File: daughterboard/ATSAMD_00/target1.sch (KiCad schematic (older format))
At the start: 0 parts

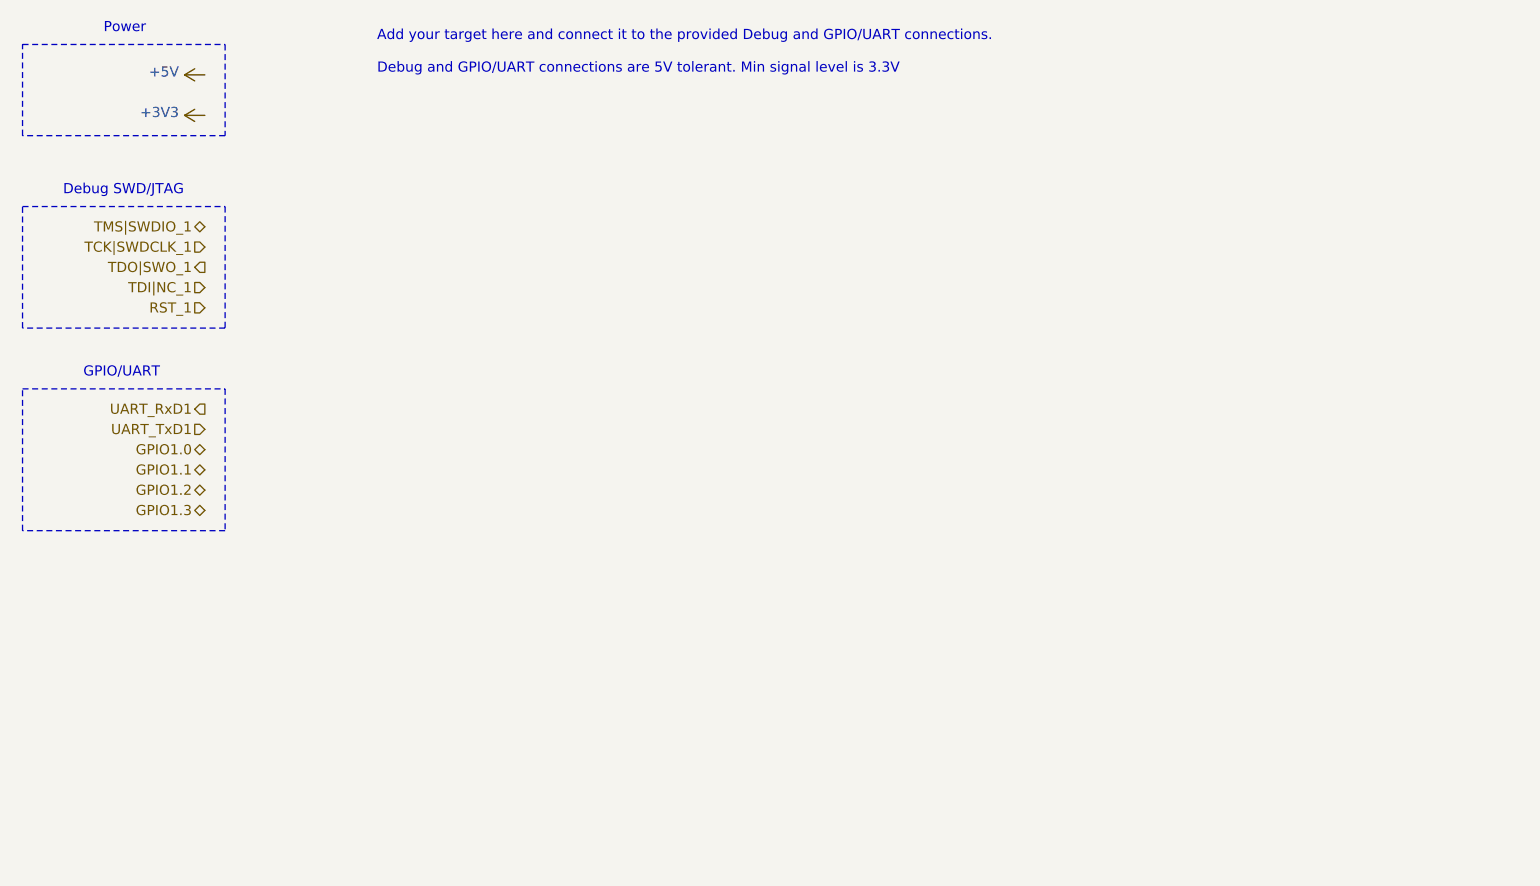
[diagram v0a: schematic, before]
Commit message: finished ATSAMD daughterboard schematics
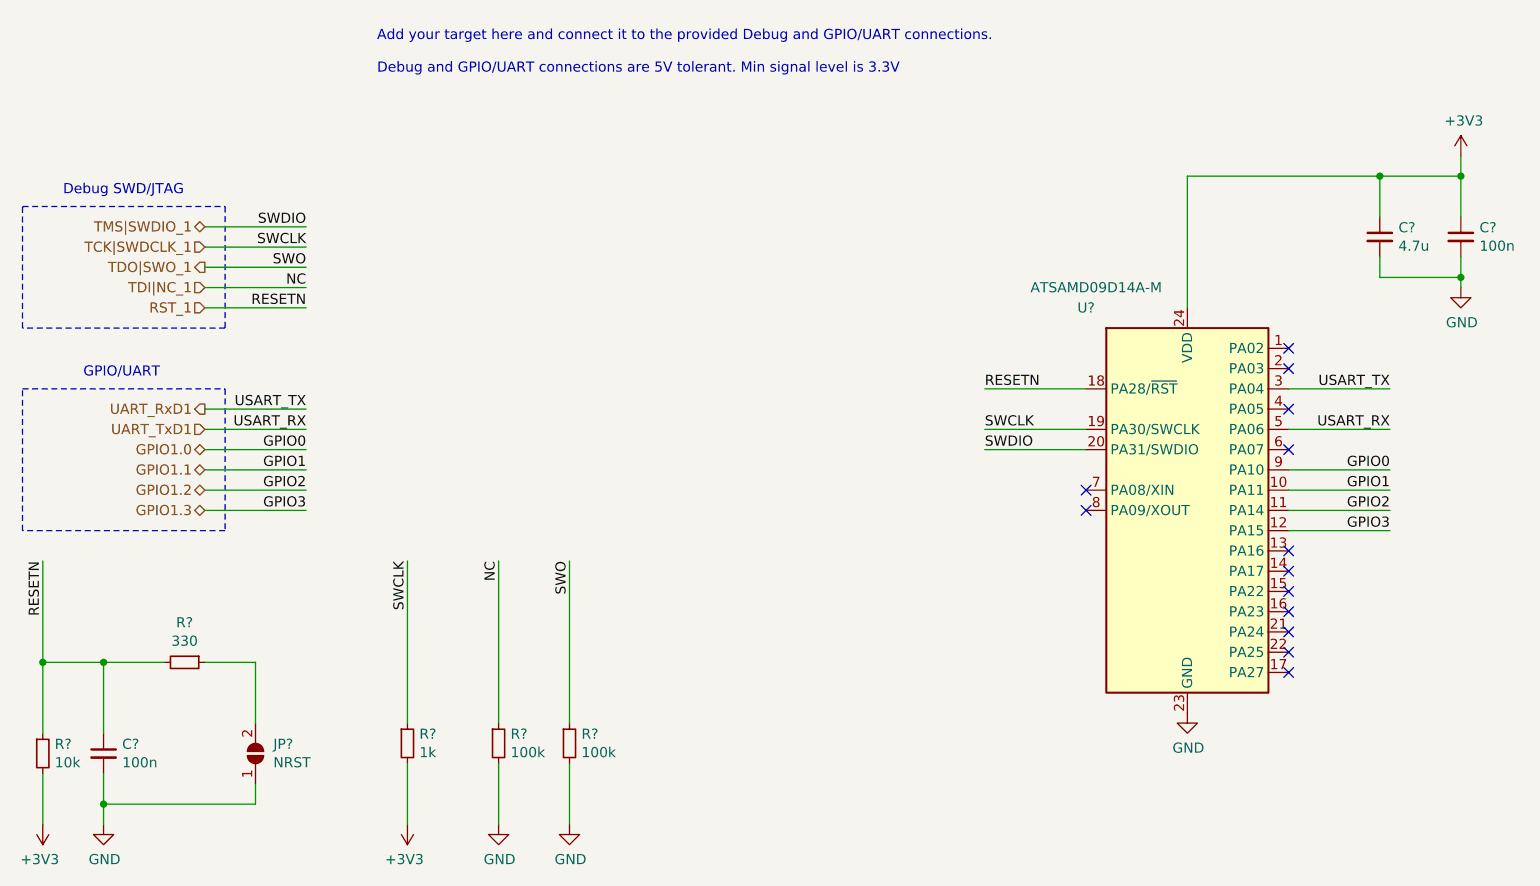
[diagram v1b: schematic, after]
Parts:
- added C?: 4.7u, symbol Device:C_Small
- added C? (x2): 100n, symbol Device:C_Small
- added JP?: NRST, symbol Jumper:SolderJumper_2_Open
- added R?: 10k, symbol Device:R_Small
- added R?: 330, symbol Device:R_Small
- added R?: 1k, symbol Device:R_Small
- added R? (x2): 100k, symbol Device:R_Small
- added U?: ATSAMD09D14A-M, Package_DFN_QFN:QFN-24-1EP_4x4mm_P0.5mm_EP2.6x2.6mm, symbol MCU_Microchip_SAMD:ATSAMD09D14A-M
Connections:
- net +3V3: now also C?.1, C?.1, R?.2, R?.2, U?.24 (VDD)
- net GPIO1.0: now also U?.9 (PA10)
- net GPIO1.1: now also U?.10 (PA11)
- net GPIO1.2: now also U?.11 (PA14)
- net GPIO1.3: now also U?.12 (PA15)
- net RST_1: now also C?.1, R?.1, R?.2, U?.18 (PA28/~RST)
- net TCK|SWDCLK_1: now also R?.1, U?.19 (PA30/SWCLK)
- net TDI|NC_1: now also R?.1
- net TDO|SWO_1: now also R?.1
- net TMS|SWDIO_1: now also U?.20 (PA31/SWDIO)
- net UART_RxD1: now also U?.3 (PA04)
- net UART_TxD1: now also U?.5 (PA06)
- new net: JP?.2 (B), R?.1
- new net GND: C?.2, C?.2, C?.2, JP?.1 (A), R?.2, R?.2, U?.23 (GND)
- no-connect marks 0 -> 13
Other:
- note removed: "Power"

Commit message: ERC on daughterboards
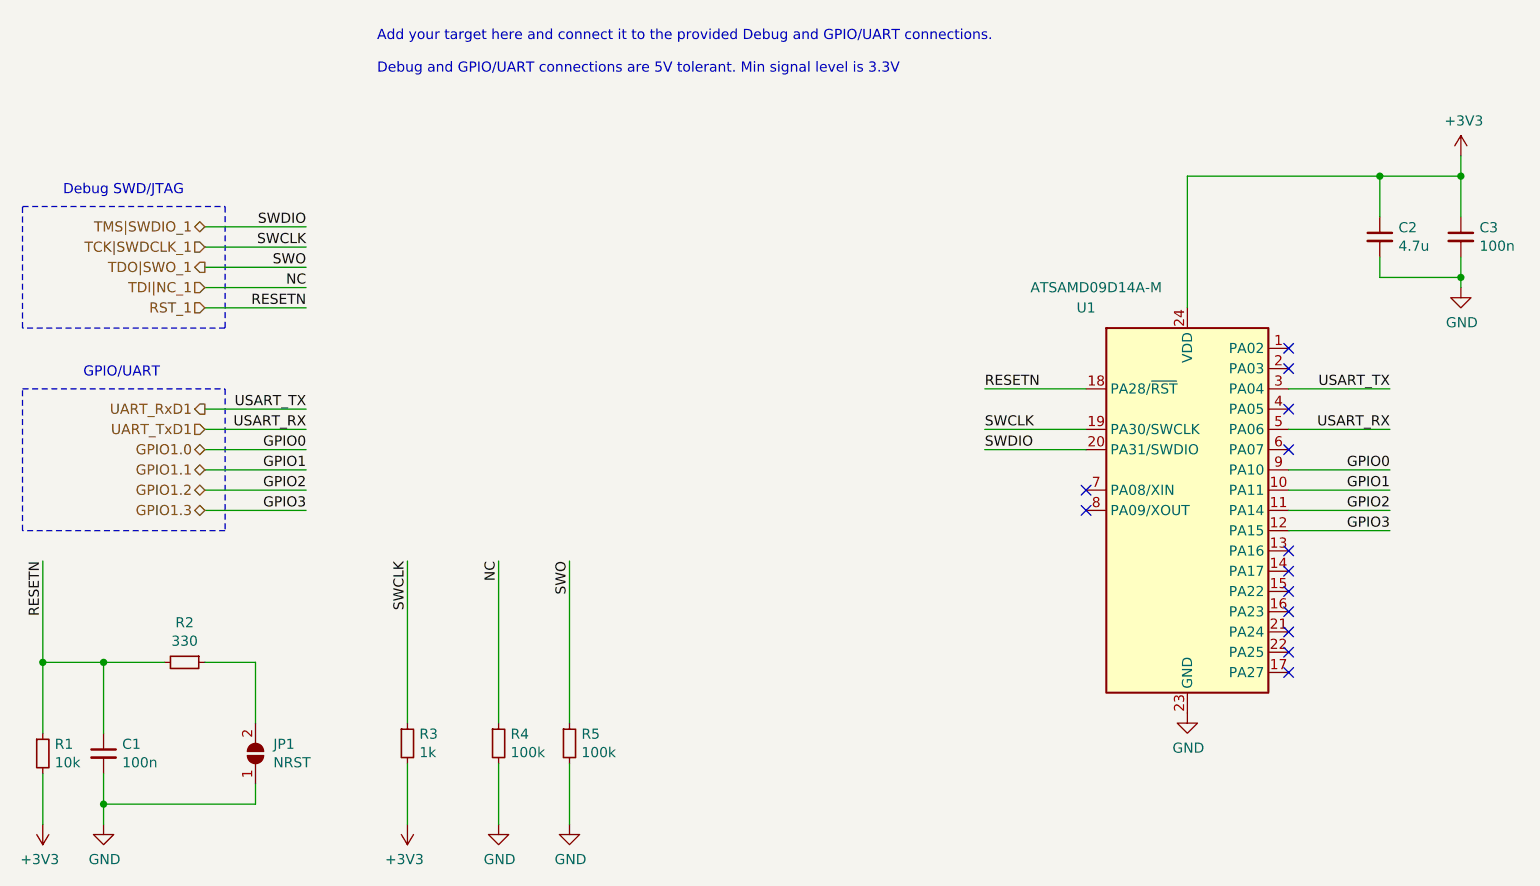
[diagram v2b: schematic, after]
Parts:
- gave numbers to parts that had none: 10
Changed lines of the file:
@@
 Add your target here and connect it to the provided Debug and GPIO/UART connections.\n\nDebug and GPIO/UART connections are 5V tolerant. Min signal level is 3.3V
 $Comp
-L MCU_Microchip_SAMD:ATSAMD09D14A-M U?
+L MCU_Microchip_SAMD:ATSAMD09D14A-M U1
 U 1 1 618B7475
 P 6450 3100
-F 0 "U?" H 5950 4100 50  0000 C CNN
+F 0 "U1" H 5950 4100 50  0000 C CNN
 F 1 "ATSAMD09D14A-M" H 6000 4200 50  0000 C CNN
 F 2 "Package_DFN_QFN:QFN-24-1EP_4x4mm_P0.5mm_EP2.6x2.6mm" H 6450 1750 50  0001 C CNN
@@
 RESETN
 $Comp
-L power:GND #PWR?
+L power:GND #PWR0116
 U 1 1 618B9185
 P 6450 4100
-F 0 "#PWR?" H 6450 3850 50  0001 C CNN
+F 0 "#PWR0116" H 6450 3850 50  0001 C CNN
 F 1 "GND" H 6455 3927 50  0000 C CNN
 F 2 "" H 6450 4100 50  0001 C CNN
@@
 AR Path="/616688D6/618BAC90" Ref="C?"  Part="1"
 AR Path="/61668514/618BAC90" Ref="C?"  Part="1"
-AR Path="/61667F91/618BAC90" Ref="C?"  Part="1"
-F 0 "C?" H 7492 1796 50  0000 L CNN
+AR Path="/61667F91/618BAC90" Ref="C2"  Part="1"
+F 0 "C2" H 7492 1796 50  0000 L CNN
 F 1 "4.7u" H 7492 1705 50  0000 L CNN
 F 2 "" H 7400 1750 50  0001 C CNN
@@
 AR Path="/616688D6/618BAC96" Ref="C?"  Part="1"
 AR Path="/61668514/618BAC96" Ref="C?"  Part="1"
-AR Path="/61667F91/618BAC96" Ref="C?"  Part="1"
-F 0 "C?" H 7892 1796 50  0000 L CNN
+AR Path="/61667F91/618BAC96" Ref="C3"  Part="1"
+F 0 "C3" H 7892 1796 50  0000 L CNN
 F 1 "100n" H 7892 1705 50  0000 L CNN
 F 2 "" H 7800 1750 50  0001 C CNN
@@
 AR Path="/616688D6/618BACA5" Ref="#PWR?"  Part="1"
 AR Path="/61668514/618BACA5" Ref="#PWR?"  Part="1"
-AR Path="/61667F91/618BACA5" Ref="#PWR?"  Part="1"
-F 0 "#PWR?" H 7800 1200 50  0001 C CNN
+AR Path="/61667F91/618BACA5" Ref="#PWR0117"  Part="1"
+F 0 "#PWR0117" H 7800 1200 50  0001 C CNN
 F 1 "+3V3" H 7815 1523 50  0000 C CNN
 F 2 "" H 7800 1350 50  0001 C CNN
@@
 	6450 1450 7400 1450
 $Comp
-L power:GND #PWR?
+L power:GND #PWR0118
 U 1 1 618BAF6F
 P 7800 2000
-F 0 "#PWR?" H 7800 1750 50  0001 C CNN
+F 0 "#PWR0118" H 7800 1750 50  0001 C CNN
 F 1 "GND" H 7805 1827 50  0000 C CNN
 F 2 "" H 7800 2000 50  0001 C CNN
@@
 RESETN
 $Comp
-L Device:R_Small R?
+L Device:R_Small R1
 U 1 1 618C06DF
 P 800 4300
-F 0 "R?" H 859 4346 50  0000 L CNN
+F 0 "R1" H 859 4346 50  0000 L CNN
 F 1 "10k" H 859 4255 50  0000 L CNN
 F 2 "" H 800 4300 50  0001 C CNN
@@
 $EndComp
 $Comp
-L Device:R_Small R?
+L Device:R_Small R2
 U 1 1 618C06E5
 P 1500 3850
-F 0 "R?" V 1304 3850 50  0000 C CNN
+F 0 "R2" V 1304 3850 50  0000 C CNN
 F 1 "330" V 1395 3850 50  0000 C CNN
 F 2 "" H 1500 3850 50  0001 C CNN
@@
 $EndComp
 $Comp
-L Device:C_Small C?
+L Device:C_Small C1
 U 1 1 618C06EB
 P 1100 4300
-F 0 "C?" H 1192 4346 50  0000 L CNN
+F 0 "C1" H 1192 4346 50  0000 L CNN
 F 1 "100n" H 1192 4255 50  0000 L CNN
 F 2 "" H 1100 4300 50  0001 C CNN
@@
 $EndComp
 $Comp
-L power:+3V3 #PWR?
+L power:+3V3 #PWR0119
 U 1 1 618C06F1
 P 800 4650
-F 0 "#PWR?" H 800 4500 50  0001 C CNN
+F 0 "#PWR0119" H 800 4500 50  0001 C CNN
 F 1 "+3V3" H 815 4823 50  0000 C CNN
 F 2 "" H 800 4650 50  0001 C CNN
@@
 	1100 3850 800  3850
 $Comp
-L power:GND #PWR?
+L power:GND #PWR0122
 U 1 1 618C06FF
 P 1100 4650
-F 0 "#PWR?" H 1100 4400 50  0001 C CNN
+F 0 "#PWR0122" H 1100 4400 50  0001 C CNN
 F 1 "GND" H 1105 4477 50  0000 C CNN
 F 2 "" H 1100 4650 50  0001 C CNN
@@
 	1100 4650 1100 4550
 $Comp
-L Jumper:SolderJumper_2_Open JP?
+L Jumper:SolderJumper_2_Open JP1
 U 1 1 618C0706
 P 1850 4300
-F 0 "JP?" V 1896 4212 50  0000 R CNN
+F 0 "JP1" V 1896 4212 50  0000 R CNN
 F 1 "NRST" V 1805 4212 50  0000 R CNN
 F 2 "" H 1850 4300 50  0001 C CNN
@@
 SWCLK
 $Comp
-L Device:R_Small R?
+L Device:R_Small R3
 U 1 1 618C0713
 P 2600 4250
-F 0 "R?" H 2659 4296 50  0000 L CNN
+F 0 "R3" H 2659 4296 50  0000 L CNN
 F 1 "1k" H 2659 4205 50  0000 L CNN
 F 2 "" H 2600 4250 50  0001 C CNN
@@
 $EndComp
 $Comp
-L power:+3V3 #PWR?
+L power:+3V3 #PWR0123
 U 1 1 618C0719
 P 2600 4650
-F 0 "#PWR?" H 2600 4500 50  0001 C CNN
+F 0 "#PWR0123" H 2600 4500 50  0001 C CNN
 F 1 "+3V3" H 2615 4823 50  0000 C CNN
 F 2 "" H 2600 4650 50  0001 C CNN
@@
 NC
 $Comp
-L Device:R_Small R?
+L Device:R_Small R4
 U 1 1 618C0722
 P 3050 4250
-F 0 "R?" H 3109 4296 50  0000 L CNN
+F 0 "R4" H 3109 4296 50  0000 L CNN
 F 1 "100k" H 3109 4205 50  0000 L CNN
 F 2 "" H 3050 4250 50  0001 C CNN
@@
 $EndComp
 $Comp
-L power:GND #PWR?
+L power:GND #PWR0130
 U 1 1 618C0728
 P 3050 4650
-F 0 "#PWR?" H 3050 4400 50  0001 C CNN
+F 0 "#PWR0130" H 3050 4400 50  0001 C CNN
 F 1 "GND" H 3055 4477 50  0000 C CNN
 F 2 "" H 3050 4650 50  0001 C CNN
@@
 SWO
 $Comp
-L Device:R_Small R?
+L Device:R_Small R5
 U 1 1 618C0731
 P 3400 4250
-F 0 "R?" H 3459 4296 50  0000 L CNN
+F 0 "R5" H 3459 4296 50  0000 L CNN
 F 1 "100k" H 3459 4205 50  0000 L CNN
 F 2 "" H 3400 4250 50  0001 C CNN
@@
 $EndComp
 $Comp
-L power:GND #PWR?
+L power:GND #PWR0131
 U 1 1 618C0737
 P 3400 4650
-F 0 "#PWR?" H 3400 4400 50  0001 C CNN
+F 0 "#PWR0131" H 3400 4400 50  0001 C CNN
 F 1 "GND" H 3405 4477 50  0000 C CNN
 F 2 "" H 3400 4650 50  0001 C CNN

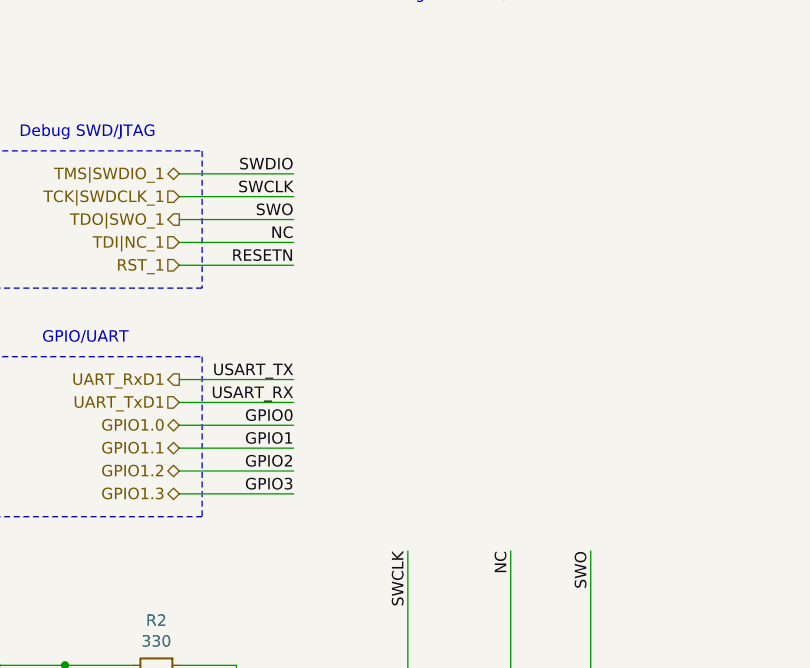
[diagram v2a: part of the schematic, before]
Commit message: added testpoints to daughterboards, updated readme
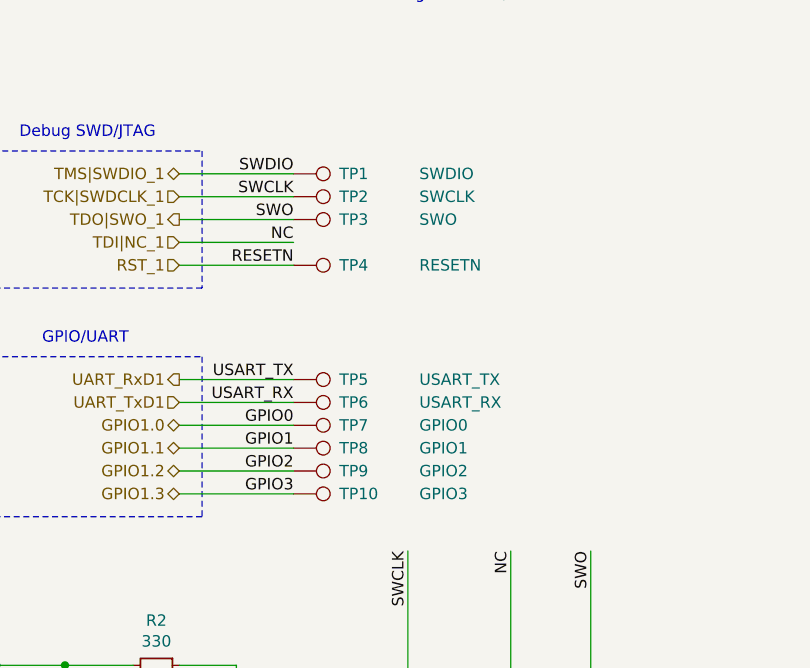
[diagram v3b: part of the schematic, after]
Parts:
- added TP1: SWDIO, symbol Connector:TestPoint
- added TP10: GPIO3, symbol Connector:TestPoint
- added TP2: SWCLK, symbol Connector:TestPoint
- added TP3: SWO, symbol Connector:TestPoint
- added TP4: RESETN, symbol Connector:TestPoint
- added TP5: USART_TX, symbol Connector:TestPoint
- added TP6: USART_RX, symbol Connector:TestPoint
- added TP7: GPIO0, symbol Connector:TestPoint
- added TP8: GPIO1, symbol Connector:TestPoint
- added TP9: GPIO2, symbol Connector:TestPoint
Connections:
- net GPIO1.0: now also TP7.1
- net GPIO1.1: now also TP8.1
- net GPIO1.2: now also TP9.1
- net GPIO1.3: now also TP10.1
- net RST_1: now also TP4.1
- net TCK|SWDCLK_1: now also TP2.1
- net TDO|SWO_1: now also TP3.1
- net TMS|SWDIO_1: now also TP1.1
- net UART_RxD1: now also TP5.1
- net UART_TxD1: now also TP6.1
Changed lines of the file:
@@
 NoConn ~ 5950 3000
 NoConn ~ 5950 3100
+$Comp
+L Connector:TestPoint TP?
+U 1 1 619256BB
+P 2100 1700
+AR Path="/616688D6/619256BB" Ref="TP?"  Part="1"
+AR Path="/61667F91/619256BB" Ref="TP1"  Part="1"
+F 0 "TP1" V 2100 1900 50  0000 L CNN
+F 1 "SWDIO" V 2100 2250 50  0000 L CNN
+F 2 "" H 2300 1700 50  0001 C CNN
+F 3 "~" H 2300 1700 50  0001 C CNN
+	1    2100 1700
+	0    1    1    0
+$EndComp
+$Comp
+L Connector:TestPoint TP?
+U 1 1 619256C1
+P 2100 1800
+AR Path="/616688D6/619256C1" Ref="TP?"  Part="1"
+AR Path="/61667F91/619256C1" Ref="TP2"  Part="1"
+F 0 "TP2" V 2100 2000 50  0000 L CNN
+F 1 "SWCLK" V 2100 2350 50  0000 L CNN
+F 2 "" H 2300 1800 50  0001 C CNN
+F 3 "~" H 2300 1800 50  0001 C CNN
+	1    2100 1800
+	0    1    1    0
+$EndComp
+$Comp
+L Connector:TestPoint TP?
+U 1 1 619256C7
+P 2100 1900
+AR Path="/616688D6/619256C7" Ref="TP?"  Part="1"
+AR Path="/61667F91/619256C7" Ref="TP3"  Part="1"
+F 0 "TP3" V 2100 2100 50  0000 L CNN
+F 1 "SWO" V 2100 2450 50  0000 L CNN
+F 2 "" H 2300 1900 50  0001 C CNN
+F 3 "~" H 2300 1900 50  0001 C CNN
+	1    2100 1900
+	0    1    1    0
+$EndComp
+$Comp
+L Connector:TestPoint TP?
+U 1 1 619256CD
+P 2100 2100
+AR Path="/616688D6/619256CD" Ref="TP?"  Part="1"
+AR Path="/61667F91/619256CD" Ref="TP4"  Part="1"
+F 0 "TP4" V 2100 2300 50  0000 L CNN
+F 1 "RESETN" V 2100 2650 50  0000 L CNN
+F 2 "" H 2300 2100 50  0001 C CNN
+F 3 "~" H 2300 2100 50  0001 C CNN
+	1    2100 2100
+	0    1    1    0
+$EndComp
+$Comp
+L Connector:TestPoint TP?
+U 1 1 619256D3
+P 2100 2600
+AR Path="/616688D6/619256D3" Ref="TP?"  Part="1"
+AR Path="/61667F91/619256D3" Ref="TP5"  Part="1"
+F 0 "TP5" V 2100 2800 50  0000 L CNN
+F 1 "USART_TX" V 2100 3150 50  0000 L CNN
+F 2 "" H 2300 2600 50  0001 C CNN
+F 3 "~" H 2300 2600 50  0001 C CNN
+	1    2100 2600
+	0    1    -1   0
+$EndComp
+$Comp
+L Connector:TestPoint TP?
+U 1 1 619256D9
+P 2100 2700
+AR Path="/616688D6/619256D9" Ref="TP?"  Part="1"
+AR Path="/61667F91/619256D9" Ref="TP6"  Part="1"
+F 0 "TP6" V 2100 2900 50  0000 L CNN
+F 1 "USART_RX" V 2100 3250 50  0000 L CNN
+F 2 "" H 2300 2700 50  0001 C CNN
+F 3 "~" H 2300 2700 50  0001 C CNN
+	1    2100 2700
+	0    1    -1   0
+$EndComp
+$Comp
+L Connector:TestPoint TP?
+U 1 1 619256DF
+P 2100 2800
+AR Path="/616688D6/619256DF" Ref="TP?"  Part="1"
+AR Path="/61667F91/619256DF" Ref="TP7"  Part="1"
+F 0 "TP7" V 2100 3000 50  0000 L CNN
+F 1 "GPIO0" V 2100 3350 50  0000 L CNN
+F 2 "" H 2300 2800 50  0001 C CNN
+F 3 "~" H 2300 2800 50  0001 C CNN
+	1    2100 2800
+	0    1    -1   0
+$EndComp
+$Comp
+L Connector:TestPoint TP?
+U 1 1 619256E5
+P 2100 2900
+AR Path="/616688D6/619256E5" Ref="TP?"  Part="1"
+AR Path="/61667F91/619256E5" Ref="TP8"  Part="1"
+F 0 "TP8" V 2100 3100 50  0000 L CNN
+F 1 "GPIO1" V 2100 3450 50  0000 L CNN
+F 2 "" H 2300 2900 50  0001 C CNN
+F 3 "~" H 2300 2900 50  0001 C CNN
+	1    2100 2900
+	0    1    -1   0
+$EndComp
+$Comp
+L Connector:TestPoint TP?
+U 1 1 619256EB
+P 2100 3000
+AR Path="/616688D6/619256EB" Ref="TP?"  Part="1"
+AR Path="/61667F91/619256EB" Ref="TP9"  Part="1"
+F 0 "TP9" V 2100 3200 50  0000 L CNN
+F 1 "GPIO2" V 2100 3550 50  0000 L CNN
+F 2 "" H 2300 3000 50  0001 C CNN
+F 3 "~" H 2300 3000 50  0001 C CNN
+	1    2100 3000
+	0    1    -1   0
+$EndComp
+$Comp
+L Connector:TestPoint TP?
+U 1 1 619256F1
+P 2100 3100
+AR Path="/616688D6/619256F1" Ref="TP?"  Part="1"
+AR Path="/61667F91/619256F1" Ref="TP10"  Part="1"
+F 0 "TP10" V 2100 3300 50  0000 L CNN
+F 1 "GPIO3" V 2100 3650 50  0000 L CNN
+F 2 "" H 2300 3100 50  0001 C CNN
+F 3 "~" H 2300 3100 50  0001 C CNN
+	1    2100 3100
+	0    1    -1   0
+$EndComp
 $EndSCHEMATC
